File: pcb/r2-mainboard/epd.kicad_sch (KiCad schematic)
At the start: 8 parts, among them J6 FPC-05F-50PH20

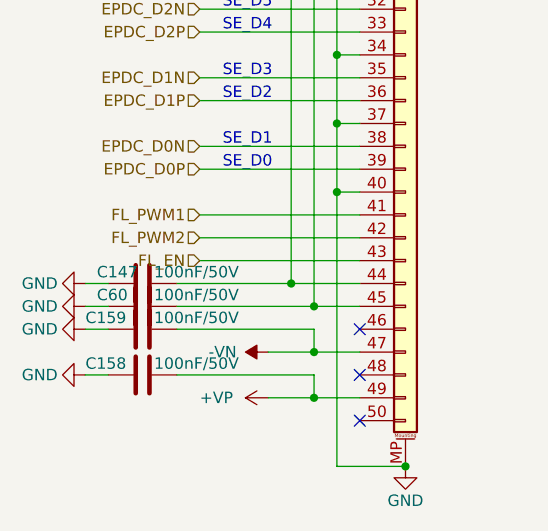
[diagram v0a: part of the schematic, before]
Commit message: R2: the six approved edits, and one of them was already done
Owner-approved 2026-08-19, KiCad closed for the pass.

1. R225 22k -> 20.5K/1%, LCSC C57105 (0402WGF2052TCE, UNI-ROYAL, the
   family the rest of the board already uses). Rendered and checked:
   R224 390k over R225 20.5k with R213 100k injecting VGH_DAC, so
   20.5||100 = 17.01k and VGH = 1.2 x (1 + 390/17.01) = 28.71 V at
   DAC = 0 -- exactly epd-port.md 10.3's target.
2. The five sense-divider caps that carried codes for the wrong
   capacitance -> C1523 (0402B102K500NT, 1 nF 50 V X7R, JLC Basic,
   5.3 M stock). One part covers both the 25 V and 50 V positions.
2b. R88/R224 -> C54920667 (HRC0402F3903DNTO, 390k 1%, 20 k stock).
   C25782 had 14 units against two per board. The owner found this one;
   both obvious alternatives were traps -- C23150 is 0603, and C44937
   is 3.9 ohm despite "390K" in its part number.
3. C147 set DNP rather than deleted. panel.md 7 had already ruled that
   J6.7/J6.44 stay; that covered the pins but not the capacitor on the
   dead net. DNP drops it from placement, keeps the topology of a frozen
   sheet untouched, and leaves the footprint if a future panel drives
   the rail. in_bom stays yes -- that is this board's convention for all
   13 DNP parts, so they show up flagged rather than vanishing.
4. Ten duplicate #PWR references renumbered to #PWR1112-1121 on the
   battery sheet, which was the colliding side in every case.
5. J3 was already deleted on 2026-08-15. No work needed.
6. Specter -> Reflow across 22 files: 14 sheets, 7 generators, the
   project file. .history/ deliberately untouched.

Verified as one change: netlist before and after has 518 nets with
identical pin membership, and epd_power and epd were rendered to PNG and
inspected.

Docs updated to match: epd-port.md 10 is applied rather than designed,
frontlight.md 1 loses the "9 in series is inferred" hedge (the vendor
listing confirms 2 x 9), and io-expansion.md 4's "only guess on this
sheet" is resolved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
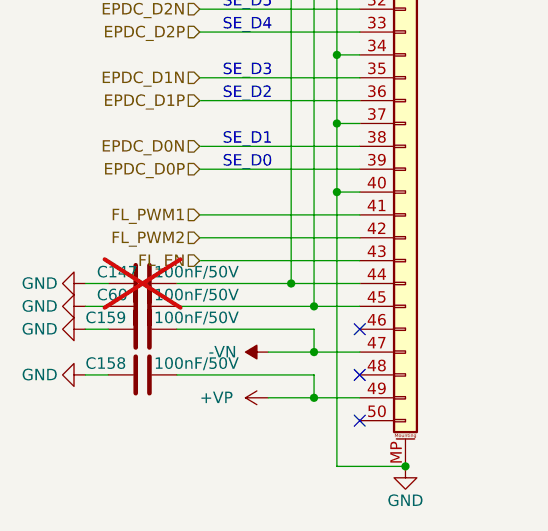
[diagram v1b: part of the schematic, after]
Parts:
- C147: BOM Comments (none) -> DNP - decouples +5V2_FL, which has no source on this panel 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; now not fitted
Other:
- title: Glider-R2 / Specter mainboard -> Glider-R2 / Reflow mainboard
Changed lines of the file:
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@@
 	(paper "A4")
 	(title_block
-		(title "Glider-R2 / Specter mainboard")
+		(title "Glider-R2 / Reflow mainboard")
 		(date "2026-08-07")
 		(rev "A")
@@
 		(on_board yes)
 		(in_pos_files yes)
-		(dnp no)
+		(dnp yes)
 		(property "Reference" "C147"
 			(at 105.41 151.13 90)
@@
 			)
 		)
+		(property "BOM Comments" "DNP - decouples +5V2_FL, which has no source on this panel (panel.md, J6.7/J6.44 unused). Footprint kept in case a future panel drives it." (at 0 0 0)
+			(effects
+				(font
+					(size 1.27 1.27)
+				)
+				(hide yes)
+			)
+		)
